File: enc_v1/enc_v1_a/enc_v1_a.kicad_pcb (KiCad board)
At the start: 2 copper layers, 24 x 15.5 mm, 6 parts, among them J2 Conn_01x09, U1 AS5047P-ATSM

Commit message: Connector changed
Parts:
- removed J2: Conn_01x09, Header:MOLEX_530480910
- added J1: 530481010, Header:CONN10_530481010_MOL, B.Cu at (137.2, 105.1)
- moved C1 32.0 mm to (154.5, 96.6)
- moved G*** 32.0 mm to (153.3, 99.3)
- moved REF** 32.0 mm to (139.3, 108.8)
- moved U1 32.0 mm to (154.8, 101.3)
- moved REF** 32.0 mm to (145.3, 102.9)
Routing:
- net /CLK: track 14.5 -> 15.8 mm
- net /W/PWM: track 16.0 -> 17.0 mm, vias 0 -> 1
- net /A: track 17.7 -> 18.6 mm
- net 3v3: track 11.7 -> 12.6 mm
- net GND: vias 8 -> 10

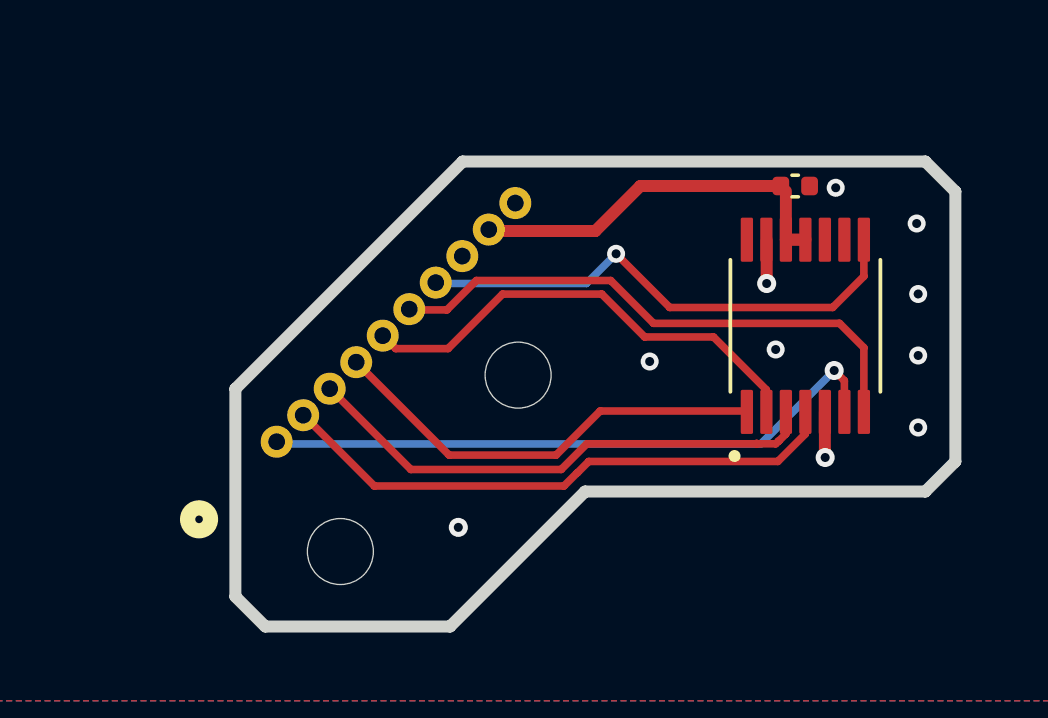
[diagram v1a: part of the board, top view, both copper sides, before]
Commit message: Connector footprint updated, fab files generated
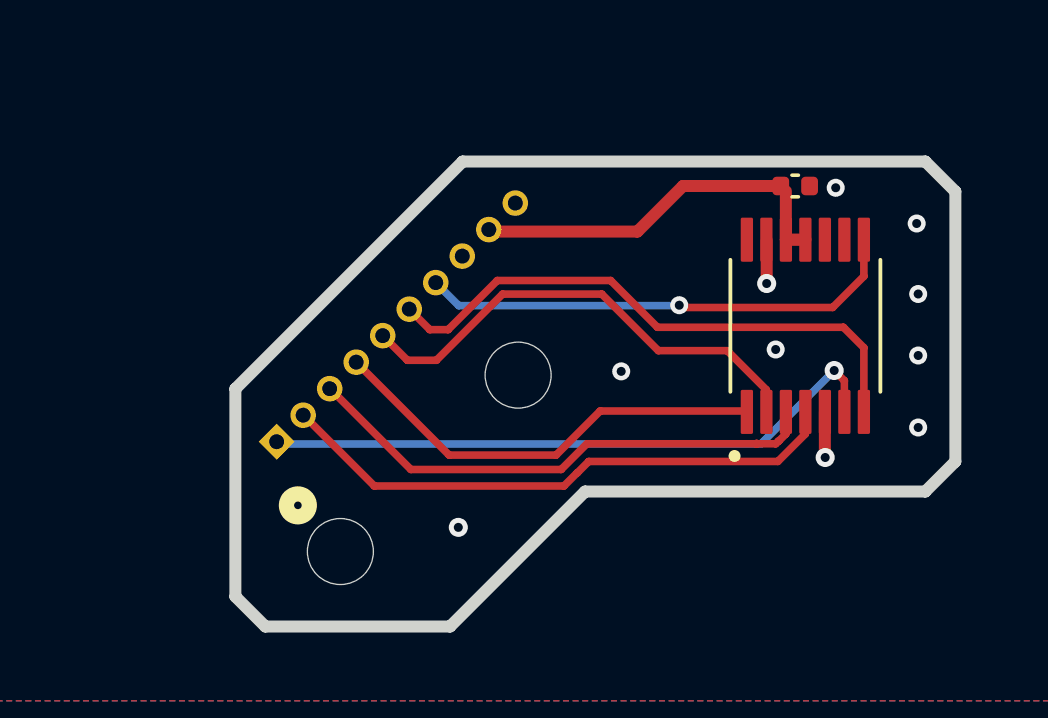
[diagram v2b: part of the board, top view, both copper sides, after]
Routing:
- net /W/PWM: track 17.0 -> 16.2 mm
- net /A: track 18.6 -> 19.1 mm
